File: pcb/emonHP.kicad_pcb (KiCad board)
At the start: 4 copper layers, 55 x 40 mm, 66 parts, among them J1 USB_C_Receptacle_USB2.0, J3 Screw_Terminal_01x03, J4 Screw_Terminal_01x02, J5 Screw_Terminal_01x02, J6 Screw_Terminal_01x03, J7 SJ-3524-SMT-TR, J8 Conn_ARM_JTAG_SWD_10, Q1 BC846, Q2 BSS84, Q3 BC846, SW1 SW_Push, U1 THVD1400D, U2 LM4040DBZ-5, U3 USBLC6-2P6, U4 AP2112K-3.3, U5 LM2733XMF, U6 ATSAMD21E15A-M, U7 MC33072

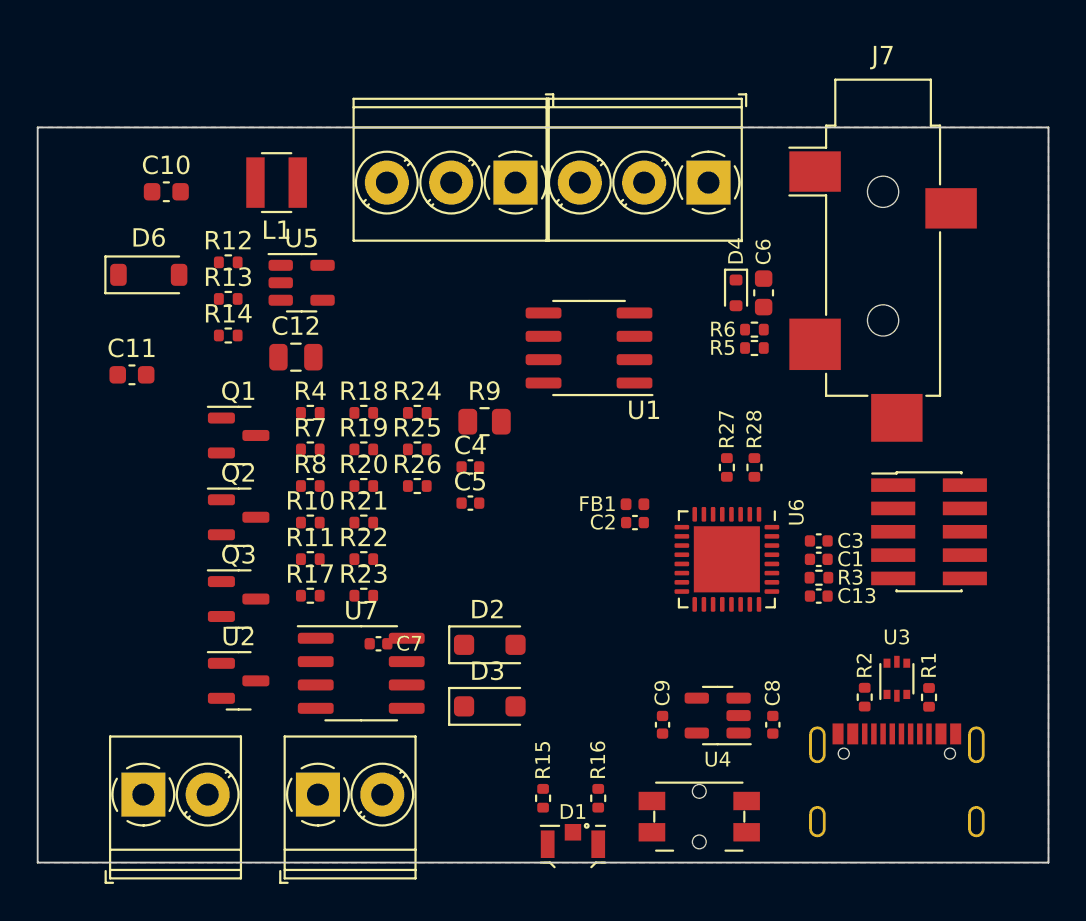
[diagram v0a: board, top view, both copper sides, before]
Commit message: * Work in progress
  - Add generate script
  - Add switch model
  - Start routing
  - Tidy schematic
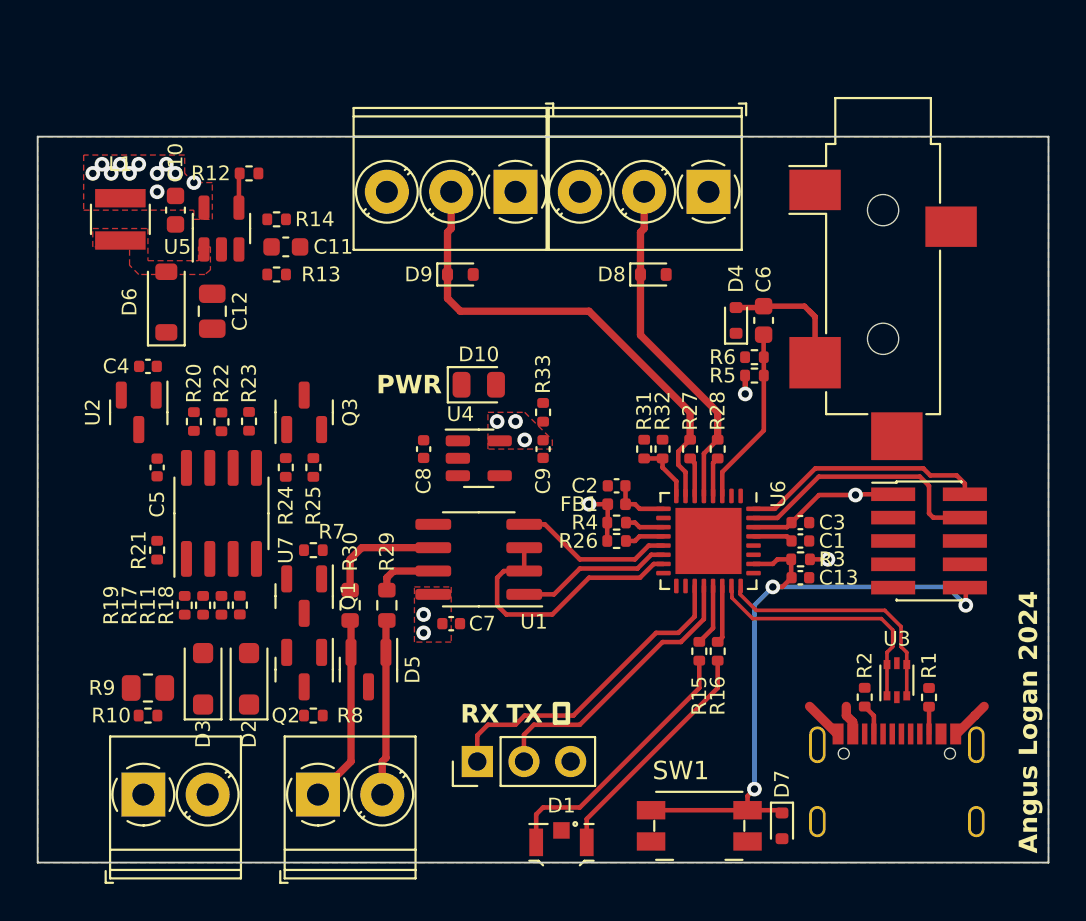
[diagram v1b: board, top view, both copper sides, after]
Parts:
- added D10: LED, LED_SMD:LED_0805_2012Metric, F.Cu at (124.0, 74.0)
- added D5: CDSOT23-SM712, Package_TO_SOT_SMD:SOT-23, F.Cu at (118.0, 89.5)
- added D7: ESD5Z3.3T5G, Diode_SMD:D_SOD-523, F.Cu at (140.5, 98.0)
- added D8: ESD5Z3.3T5G, Diode_SMD:D_SOD-523, F.Cu at (133.5, 68.0)
- added D9: ESD5Z3.3T5G, Diode_SMD:D_SOD-523, F.Cu at (123.0, 68.0)
- added J2: Conn_01x03, Connector_PinHeader_2.54mm:PinHeader_1x03_P2.54mm_Vertical, F.Cu at (123.9, 94.5)
- added R29: 10R, Resistor_SMD:R_0603_1608Metric, F.Cu at (119.0, 86.0)
- added R30: 10R, Resistor_SMD:R_0603_1608Metric, F.Cu at (117.0, 86.0)
- added R31: 20K, Resistor_SMD:R_0402_1005Metric, F.Cu at (133.0, 77.5)
- added R32: 1K, Resistor_SMD:R_0402_1005Metric, F.Cu at (134.0, 77.5)
- added R33: 1K, Resistor_SMD:R_0402_1005Metric, F.Cu at (127.5, 75.5)
- SW1: footprint Button_Switch_SMD:Panasonic_EVQPUM_EVQPUD -> Button_Switch_SMD:Panasonic_EVQPUJ_EVQPUA
- moved C8 24.2 mm to (121.0, 77.5), turned to -90 degrees
- moved R9 23.4 mm to (106.0, 90.5), turned to 180 degrees
- moved U4 19.1 mm to (124.0, 78.0), turned to 0 degrees
- moved C4 18.4 mm to (106.0, 73.0), turned to 180 degrees
- moved R4 17.7 mm to (131.5, 81.5), turned to 180 degrees
- moved C5 17.2 mm to (106.5, 78.5), turned to -90 degrees
- moved C9 16.3 mm to (127.5, 77.5), turned to -90 degrees
- moved D3 15.7 mm to (109.0, 90.0), turned to 90 degrees
- moved U2 15.6 mm to (105.5, 75.5), turned to -90 degrees
- moved R10 13.7 mm to (106.0, 92.0), turned to 180 degrees
- moved D2 13.2 mm to (111.5, 90.0), turned to 90 degrees
- moved U1 13.0 mm to (124.0, 83.5)
- moved R19 12.9 mm to (108.0, 86.0), turned to 90 degrees
- moved R8 12.5 mm to (115.0, 92.0)
- moved R18 12.4 mm to (111.0, 86.0), turned to -90 degrees
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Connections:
- net Net-(R19-Pad2) renamed /mbus/DIFF_5V
- R12 pad 1: +5V -> /BOOST_EN
- R12 pad 2: Net-(U5-EN) -> GND
- U1 pad 6: /RS485_B -> Net-(U1-A)
- U1 pad 7: /RS485_A -> Net-(U1-B)
- U5 pad 4: Net-(U5-EN) -> /BOOST_EN
- U6 pad 1: /CT1 -> unconnected-(U6-PA00-Pad1)
- U6 pad 16: unconnected-(U6-PA15-Pad16) -> /BOOST_EN
- U6 pad 19: unconnected-(U6-PA18-Pad19) -> /DBG_TX
- U6 pad 2: /OW_PU0 -> unconnected-(U6-PA01-Pad2)
- U6 pad 20: unconnected-(U6-PA19-Pad20) -> /DBG_RX
- U6 pad 3: /OPA0 -> /CT1
- U6 pad 4: /OW_PU1 -> /OW_PU0
- U6 pad 5: /OPA1 -> /OPA0
- U6 pad 6: unconnected-(U6-PA05-Pad6) -> /OW_PU1
- U6 pad 7: unconnected-(U6-PA06-Pad7) -> /OPA1
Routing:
- net +3V3: track 0.00 -> 52.2 mm, vias 0 -> 7
- net /~{RESET}: track 0.00 -> 36.2 mm, vias 0 -> 3
- net /OPA1: track 0.00 -> 26.6 mm
- net /OPA0: track 0.00 -> 18.7 mm
- net /DBG_TX: track 0.00 -> 17.6 mm
- net /DBG_RX: track 0.00 -> 15.7 mm
- net Net-(D1-K2): track 0.00 -> 14.8 mm
- net /RS485_DE: track 0.00 -> 14.8 mm
- net /SWCLK: track 0.00 -> 14.2 mm
- net /USB-DP: track 0.00 -> 13.8 mm
- net /USB-DN: track 0.00 -> 13.8 mm
- net /SWDIO: track 0.00 -> 13.3 mm
- net Net-(D1-K1): track 0.00 -> 12.9 mm
- net /RS485_B: track 0.00 -> 10.2 mm
- net /CT1: track 0.00 -> 9.72 mm
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- added copper zone on F.Cu, net +3V3
- added copper zone on In2.Cu, net +3V3
- added copper zone on F.Cu, net +5V
- added copper zone on In2.Cu, net +5V
- added copper zone on F.Cu, net /boost/BOOST_SW
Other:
- board size 55 x 40 mm -> 55 x 39.5 mm
- board text added: "Angus Logan 2024"
- board text added: "PWR"
- board text added: "RX"
- board text added: "TX"
- board text added: "emonHP OpenEnergyMonitor.org"
- board text added: "⏚"

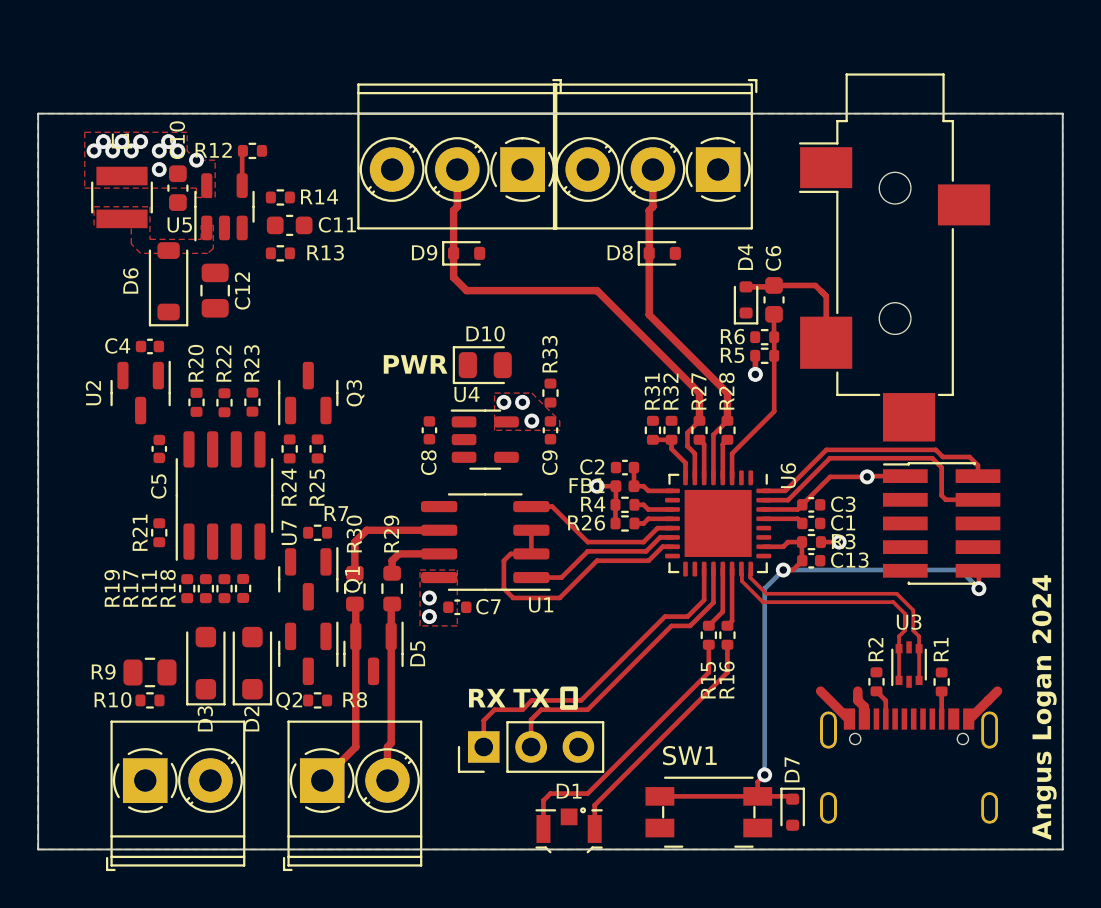
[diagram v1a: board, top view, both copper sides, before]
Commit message: * [0.1-dev] Voltage good
  - Add 36V voltage good detection
  - Add all 3D models
  - Correct footprint for front LED
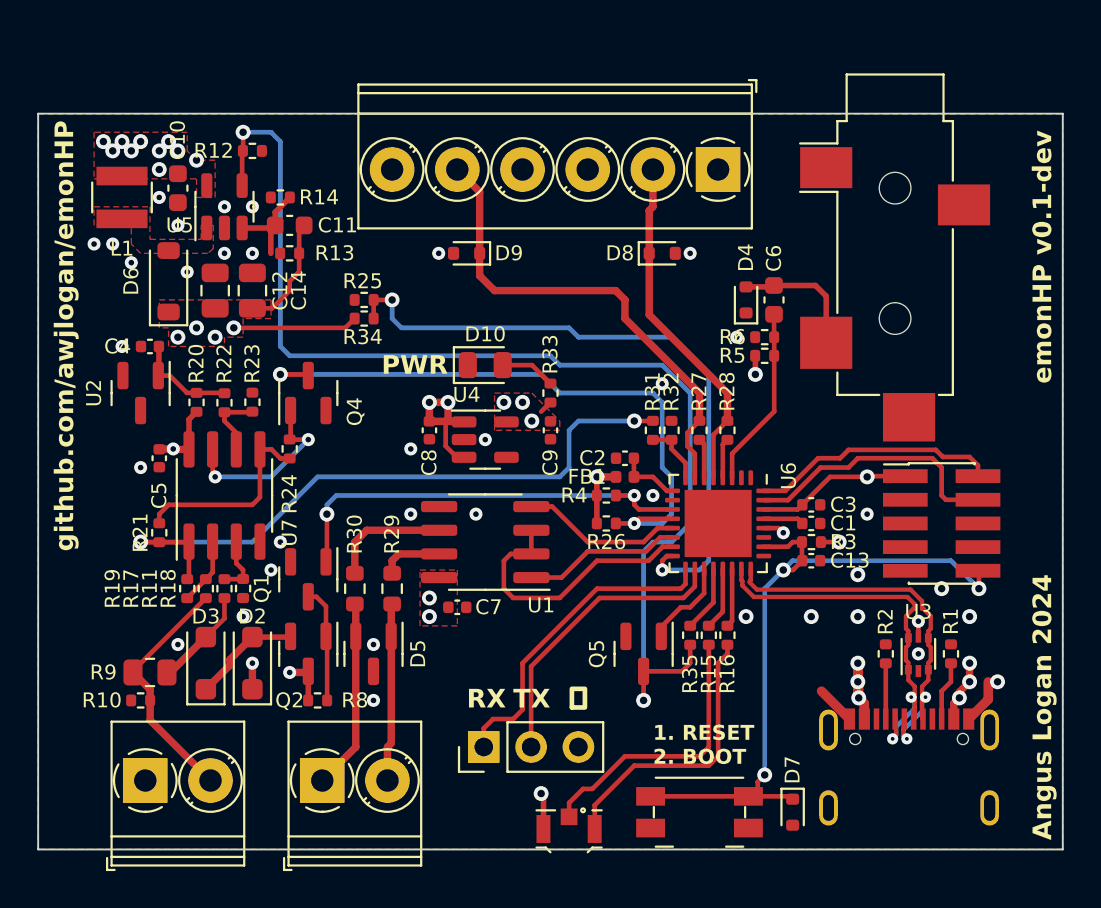
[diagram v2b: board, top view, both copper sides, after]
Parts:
- removed J3, J6: Screw_Terminal_01x03, TerminalBlock_Phoenix:TerminalBlock_Phoenix_PT-1,5-3-3.5-H_1x03_P3.50mm_Horizontal
- removed Q3: BC846, Package_TO_SOT_SMD:SOT-23
- removed R7: 10K, Resistor_SMD:R_0402_1005Metric
- added C14: 4u7, Capacitor_SMD:C_0805_2012Metric, F.Cu at (111.5, 70.0)
- added J9: Screw_Terminal_01x06, TerminalBlock_Phoenix:TerminalBlock_Phoenix_PT-1,5-6-3.5-H_1x06_P3.50mm_Horizontal, F.Cu at (136.5, 63.5)
- added Q4: Q_NPN_BEC_BRT, Package_TO_SOT_SMD:SOT-23, F.Cu at (114.5, 75.5)
- added Q5: Q_NPN_BEC_BRT, Package_TO_SOT_SMD:SOT-23, F.Cu at (132.5, 89.5)
- added R34: 180K, Resistor_SMD:R_0402_1005Metric, F.Cu at (117.5, 71.5)
- added R35: 3K3, Resistor_SMD:R_0402_1005Metric, F.Cu at (135.0, 88.5)
- D1: value LED_Dual_KAK -> LTST-S326KGJRKT; footprint LED_SMD:LED_LiteOn_LTST-S326 -> ltst-s326:LTST-S326
- Q1: value BC846 -> Q_NPN_BEC_BRT
- R25: value 20K -> 13K3
- R5: value 47K -> 100K
- moved R25 8.38 mm to (117.5, 70.5), turned to 180 degrees
- moved R1 1.59 mm to (149.0, 89.5)
- moved R2 1.58 mm to (145.5, 89.5)
- moved R4 1.12 mm to (130.5, 81.0)
- moved R26 1.00 mm to (130.5, 82.5)
- moved U3 0.76 mm to (147.2, 89.5)
- moved C2 0.50 mm to (131.5, 79.0)
- moved C5 0.50 mm to (106.5, 79.0)
- moved FB1 0.50 mm to (131.5, 80.0)
- moved R10 0.50 mm to (105.5, 92.0)
- moved R13 0.50 mm to (113.5, 68.0)
- moved SW1 0.50 mm to (135.5, 98.0)
- turned D9 to 180 degrees
- turned L1 to 90 degrees
- turned R24 to 90 degrees
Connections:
- D1 pad 2: +3V3 -> +5V
- L1 pad 1: +5V -> /boost/BOOST_SW
- L1 pad 2: /boost/BOOST_SW -> +5V
- Q1 pad 1: Net-(Q1-B) -> /MBUS_TX
- R12 pad 1: /BOOST_EN -> /BOOST_EN_PROT
- R24 pad 2: Net-(R24-Pad2) -> Net-(Q4-B)
- R25 pad 1: Net-(Q3-B) -> /36V_RG
- R25 pad 2: Net-(R24-Pad2) -> GND
- U5 pad 4: /BOOST_EN -> /BOOST_EN_PROT
- U6 pad 16: /BOOST_EN -> /36V_RG
- U6 pad 17: unconnected-(U6-PA16-Pad17) -> /DBG_TX
- U6 pad 18: unconnected-(U6-PA17-Pad18) -> /DBG_RX
- U6 pad 19: /DBG_TX -> /OC_CMP_OUT
- U6 pad 20: /DBG_RX -> /BOOST_EN
- U7 pad 7: Net-(R24-Pad2) -> Net-(Q4-B)
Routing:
- net /BOOST_EN_PROT: track 0.00 -> 62.4 mm, vias 0 -> 2
- net /mbus/DIFF_5V: track 0.00 -> 35.8 mm, vias 0 -> 2
- net /36V_RG: track 0.00 -> 35.1 mm, vias 0 -> 2
- net /MBUS_RX: track 2.14 -> 34.1 mm, vias 0 -> 2
- net +5V: track 1.64 -> 31.1 mm, vias 13 -> 22
- net /MBUS_TX: track 2.14 -> 23.4 mm, vias 0 -> 2
- net /36V: track 0.00 -> 20.6 mm, vias 0 -> 7
- net /MBUS_A: track 0.00 -> 13.1 mm
- net Net-(U7B-+): track 0.00 -> 10.6 mm
- net Net-(Q4-B): track 0.00 -> 9.85 mm, vias 0 -> 2
- net /USB-DN: track 13.8 -> 21.4 mm, vias 0 -> 2
- net /USB-DP: track 13.8 -> 21.4 mm, vias 0 -> 2
- net Net-(Q1-C): track 0.00 -> 6.15 mm
- net Net-(D2-A): track 0.00 -> 5.85 mm
- net Net-(U2-K): track 0.00 -> 5.45 mm
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- added copper zone on F.Cu, net /36V
- added copper zone on In2.Cu, net /36V
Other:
- board text added: "1. RESET 2. BOOT"
- board text added: "emonHP v0.1-dev"
- board text added: "github.com/awjlogan/emonHP"

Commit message: * [0.1-dev] Add git commit references and README
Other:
- board text added: "gitrev"
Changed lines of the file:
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@@
   (gr_line (start 155 100) (end 155 60.5)
     (stroke (width 0.1) (type default)) (layer "Edge.Cuts"))
-  (gr_text "github.com/awjlogan/emonHP" (at 102 84 90) (layer "F.SilkS")
+  (gr_text "github.com/awjlogan/emonHP" (at 101.5 99.5 90) (layer "F.SilkS")
     (effects (font (size 1 1) (thickness 0.25) bold) (justify left bottom))
   )
@@
     (effects (font (size 1 1) (thickness 0.25) bold) (justify left bottom))
   )
+  (gr_text "gitrev" (at 101.5 66 90) (layer "F.SilkS")
+    (effects (font (size 1 1) (thickness 0.25) bold) (justify left bottom))
+  )

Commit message: * Swap reset button for cheap onboard
  - Can access bootloader from serial, no need for front panel
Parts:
- SW1: footprint Button_Switch_SMD:Panasonic_EVQPUJ_EVQPUA -> Button_Switch_SMD:SW_Tactile_SPST_NO_Straight_CK_PTS636Sx25SMTRLFS
- moved D7 9.12 mm to (142.0, 89.0), turned to 0 degrees
- moved R15 7.57 mm to (135.0, 96.0)
- moved R16 7.57 mm to (136.0, 96.0)
- moved D1 6.50 mm to (135.0, 98.9)
- moved SW1 6.40 mm to (139.5, 93.0), turned to 90 degrees
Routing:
- net Net-(D1-K2): track 15.0 -> 1.74 mm
- net /~{RESET}: track 36.3 -> 23.5 mm
- net Net-(D1-K1): track 15.3 -> 2.55 mm
- net /LED_FP0: track 3.35 -> 11.3 mm
- net /LED_FP1: track 3.14 -> 11.1 mm
- net +5V: track 31.1 -> 27.5 mm
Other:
- board text added: "RESET"
- board text removed: "1. RESET 2. BOOT"

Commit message: [v0.1-dev] First pass on emonPi format
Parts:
- removed D1: LTST-S326KGJRKT, ltst-s326:LTST-S326
- removed D10: LED, LED_SMD:LED_0805_2012Metric
- removed D6: MBR0550, Diode_SMD:D_SOD-123
- removed J7: SJ-3524-SMT-TR, Connector_Audio:Jack_3.5mm_CUI_SJ-3524-SMT_Horizontal
- removed J8: Conn_ARM_JTAG_SWD_10, Connector_PinHeader_1.27mm:PinHeader_2x05_P1.27mm_Vertical_SMD
- removed J9: Screw_Terminal_01x06, TerminalBlock_Phoenix:TerminalBlock_Phoenix_PT-1,5-6-3.5-H_1x06_P3.50mm_Horizontal
- removed Q4, Q5: Q_NPN_BEC_BRT, Package_TO_SOT_SMD:SOT-23
- removed R12: 47K, Resistor_SMD:R_0402_1005Metric
- removed R13: 383K, Resistor_SMD:R_0402_1005Metric
- removed R14, R25: 13K3, Resistor_SMD:R_0402_1005Metric
- removed R15, R16, R21, R22: 1K, Resistor_SMD:R_0402_1005Metric
- removed R23, R24: 180K, Resistor_SMD:R_0402_1005Metric
- added C15: 100n, Capacitor_SMD:C_0402_1005Metric, F.Cu at (178.5, 140.0)
- added C18: 2u2, Capacitor_SMD:C_0603_1608Metric, F.Cu at (140.5, 100.0)
- added C19: 82p, Capacitor_SMD:C_0603_1608Metric, F.Cu at (146.5, 105.0)
- added C20: 4u7, Capacitor_SMD:C_0805_2012Metric, F.Cu at (116.5, 109.0)
- added C21: 4u7, Capacitor_SMD:C_0805_2012Metric, F.Cu at (143.0, 105.5)
- added C22: 1n, Capacitor_SMD:C_0402_1005Metric, F.Cu at (132.5, 96.0)
- added C23: 100n, Capacitor_SMD:C_0402_1005Metric, F.Cu at (126.5, 97.0)
- added C24: 100n, Capacitor_SMD:C_0402_1005Metric, F.Cu at (119.5, 91.0)
- added CN1: CONN_03SCREW, TerminalBlock_Phoenix:TerminalBlock_Phoenix_PT-1,5-3-3.5-H_1x03_P3.50mm_Horizontal, F.Cu at (108.0, 108.5)
- added CN3: Screw_Terminal_01x02, TerminalBlock_Phoenix:TerminalBlock_Phoenix_PT-1,5-2-3.5-H_1x02_P3.50mm_Horizontal, F.Cu at (108.0, 98.0)
- added CN4: CONN_03SCREW, TerminalBlock_Phoenix:TerminalBlock_Phoenix_PT-1,5-3-3.5-H_1x03_P3.50mm_Horizontal, F.Cu at (108.0, 84.0)
- added CN5: Screw_Terminal_01x02, TerminalBlock_Phoenix:TerminalBlock_Phoenix_PT-1,5-2-5.0-H_1x02_P5.00mm_Horizontal, F.Cu at (108.0, 135.5)
- added FB2: FerriteBead, Resistor_SMD:R_0402_1005Metric, F.Cu at (180.0, 140.0)
- added FD1: FIDUCIAL1X2, Fiducial:Fiducial_0.75mm_Mask1.5mm, F.Cu at (117.5, 121.0)
- added FD2: FIDUCIAL1X2, Fiducial:Fiducial_0.75mm_Mask1.5mm, F.Cu at (189.0, 146.5)
- added FD3: FIDUCIAL1X2, Fiducial:Fiducial_0.75mm_Mask1.5mm, F.Cu at (182.0, 65.5)
- added H1: MountingHole, MountingHole:MountingHole_2.7mm_M2.5, F.Cu at (128.5, 75.0)
- added H2: MountingHole, MountingHole:MountingHole_2.7mm_M2.5, F.Cu at (128.5, 124.0)
- added H3: MountingHole, MountingHole:MountingHole_2.1mm, F.Cu at (163.5, 97.0)
- added J3: USB_C_Receptacle_USB2.0, valcon-usb:CSP-USC16-TR, F.Cu at (108.5, 72.5)
- added JP1: Jumper_2_Open, Jumper:SolderJumper-2_P1.3mm_Open_TrianglePad1.0x1.5mm, F.Cu at (144.2, 96.2)
- added LED1: LED_Dual_KAK, ltst-s326:LTST-S326, F.Cu at (188.8, 134.0)
- added Q3: Q_NPN_BEC_BRT, Package_TO_SOT_SMD:SOT-23, F.Cu at (130.0, 105.0)
- added R36: 100K, Resistor_SMD:R_0402_1005Metric, F.Cu at (119.0, 97.0)
- added R37: 20K, Resistor_SMD:R_0402_1005Metric, F.Cu at (129.0, 99.0)
- added R38: 1K, Resistor_SMD:R_0402_1005Metric, F.Cu at (122.0, 97.0)
- added R39: 1K, Resistor_SMD:R_0402_1005Metric, F.Cu at (129.0, 100.5)
- added R40: 180K, Resistor_SMD:R_0402_1005Metric, F.Cu at (129.0, 102.0)
- added R41: 180K, Resistor_SMD:R_0402_1005Metric, F.Cu at (126.5, 104.0)
- added R42: 47K, Resistor_SMD:R_0402_1005Metric, F.Cu at (141.0, 117.5)
- added R43: 20K, Resistor_SMD:R_0402_1005Metric, F.Cu at (119.0, 95.5)
- added R44: 1K, Resistor_SMD:R_0402_1005Metric, F.Cu at (119.0, 94.0)
- added R45: 10R, Resistor_SMD:R_0603_1608Metric, F.Cu at (114.0, 90.5)
- added R46: 10R, Resistor_SMD:R_0603_1608Metric, F.Cu at (114.0, 84.5)
- added R7: 10K, Resistor_SMD:R_0402_1005Metric, F.Cu at (167.5, 118.5)
- added SMA1: SMACONNECTOR, Connector_Coaxial:SMA_Amphenol_132203-12_Horizontal, F.Cu at (185.5, 141.0)
- added SW2: SW_Push, Button_Switch_SMD:SW_Tactile_SPST_NO_Straight_CK_PTS636Sx25SMTRLFS, F.Cu at (145.5, 89.5)
- added TP1: TestPoint, TestPoint:TestPoint_Pad_D1.0mm, F.Cu at (182.0, 130.5)
- added TP4: TestPoint, TestPoint:TestPoint_Pad_D1.0mm, F.Cu at (183.0, 116.5)
- added TP5: TestPoint, TestPoint:TestPoint_Pad_D1.0mm, F.Cu at (133.5, 129.0)
- added TP6: TestPoint, TestPoint:TestPoint_Pad_D1.0mm, F.Cu at (184.0, 130.5)
- added TP7: TestPoint, TestPoint:TestPoint_Pad_D1.0mm, F.Cu at (123.5, 130.5)
- added TP8: TestPoint, TestPoint:TestPoint_Pad_D1.0mm, F.Cu at (180.5, 107.5)
- added U10: SN74LVC1T45DRL, Package_TO_SOT_SMD:SOT-563, F.Cu at (125.0, 91.5)
- added U8: THVD1400D, Package_SO:SOIC-8_3.9x4.9mm_P1.27mm, F.Cu at (121.5, 87.5)
- added U9: USBLC6-2P6, Package_TO_SOT_SMD:SOT-666, F.Cu at (116.2, 72.8)
- C1, C8, C9: value 1u -> 100n
- C10: value 2u2 -> 100n; footprint Capacitor_SMD:C_0603_1608Metric -> Capacitor_SMD:C_0402_1005Metric
- C11: value 82p -> 100n; footprint Capacitor_SMD:C_0603_1608Metric -> Capacitor_SMD:C_0402_1005Metric
- C12: value 4u7 -> 1u; footprint Capacitor_SMD:C_0805_2012Metric -> Capacitor_SMD:C_0402_1005Metric
- C13, C2, C5, C7: value 100n -> 2u2; footprint Capacitor_SMD:C_0402_1005Metric -> Capacitor_SMD:C_0603_1608Metric
- C14: value 4u7 -> 2u2; footprint Capacitor_SMD:C_0805_2012Metric -> Capacitor_SMD:C_0603_1608Metric
- C3: value 100n -> 10u; footprint Capacitor_SMD:C_0402_1005Metric -> Capacitor_SMD:C_0603_1608Metric
- C4: value 1n -> 2u2; footprint Capacitor_SMD:C_0402_1005Metric -> Capacitor_SMD:C_0603_1608Metric
- C6: value 10uF -> 100n; footprint Capacitor_SMD:C_0603_1608Metric -> Capacitor_SMD:C_0402_1005Metric
- D2: value BZT52C12 -> ESD5Z3.3T5G; footprint Diode_SMD:D_SOD-123F -> Diode_SMD:D_SOD-523
- D3: value BZT52C2V7 -> ESD5Z3.3T5G; footprint Diode_SMD:D_SOD-123F -> Diode_SMD:D_SOD-523
- D4: value 5V -> ESD5Z3.3T5G
- D5: value CDSOT23-SM712 -> SM712_SOT23
- D7: value ESD5Z3.3T5G -> MBR0550; footprint Diode_SMD:D_SOD-523 -> Diode_SMD:D_SOD-123
- D8: value ESD5Z3.3T5G -> BZT52C12; footprint Diode_SMD:D_SOD-523 -> Diode_SMD:D_SOD-123F
- D9: value ESD5Z3.3T5G -> BZT52C2V7; footprint Diode_SMD:D_SOD-523 -> Diode_SMD:D_SOD-123F
- FB1: value FerriteBead_Small -> FerriteBead; footprint Inductor_SMD:L_0402_1005Metric -> Resistor_SMD:R_0402_1005Metric
- J1: value USB_C_Receptacle_USB2.0 -> CONN_04PTH; footprint valcon-usb:CSP-USC16-TR -> Connector_PinSocket_2.54mm:PinSocket_1x04_P2.54mm_Vertical
- J2: value Conn_01x03 -> CONN_04PTH; footprint Connector_PinHeader_2.54mm:PinHeader_1x03_P2.54mm_Vertical -> Connector_PinSocket_2.54mm:PinSocket_1x04_P2.54mm_Vertical
- J4: value Screw_Terminal_01x02 -> Conn_ARM_JTAG_SWD_10; footprint TerminalBlock_Phoenix:TerminalBlock_Phoenix_PT-1,5-2-3.5-H_1x02_P3.50mm_Horizontal -> Connector_PinHeader_1.27mm:PinHeader_2x05_P1.27mm_Vertical_SMD
- J5: value Screw_Terminal_01x02 -> Conn_02x20_Odd_Even; footprint TerminalBlock_Phoenix:TerminalBlock_Phoenix_PT-1,5-2-3.5-H_1x02_P3.50mm_Horizontal -> RPi-SMD:REF-182665
- Q2: value BSS84 -> FDN5618P
- R1: value 5K1 -> 4K7
- R10: value 100K -> 1K
- R11: value 20K -> 10K
- R17: value 20K -> 47K
- R18, R19: value 100K -> 4K7
- R2: value 5K1 -> 37.4K; footprint Resistor_SMD:R_0402_1005Metric -> Resistor_SMD:R_2512_6332Metric
- R20: value 20K -> 37.4K; footprint Resistor_SMD:R_0402_1005Metric -> Resistor_SMD:R_2512_6332Metric
- R27: value 3K3 -> 383K
- R28: value 3K3 -> 13K3
- R29, R30: value 10R -> 47K; footprint Resistor_SMD:R_0603_1608Metric -> Resistor_SMD:R_0402_1005Metric
- R3: value 10K -> 1K
- R31: value 20K -> 100R; footprint Resistor_SMD:R_0402_1005Metric -> Resistor_SMD:R_0805_2012Metric
- R32: value 1K -> 100K
- R33: value 1K -> 20K
- R34: value 180K -> 20K
- R35: value 3K3 -> 100K
- R4: value 47K -> 5K1
- R5: value 100K -> 5K1
- R6, R8: value 47K -> 1K
- R9: value 100R -> 1K; footprint Resistor_SMD:R_0805_2012Metric -> Resistor_SMD:R_0402_1005Metric
- SW1: footprint Button_Switch_SMD:SW_Tactile_SPST_NO_Straight_CK_PTS636Sx25SMTRLFS -> Button_Switch_THT:SW_PUSH_6mm
- U1: value THVD1400D -> HCPL-3700M; footprint Package_SO:SOIC-8_3.9x4.9mm_P1.27mm -> Package_DIP:SMDIP-8_W7.62mm
- U2: value LM4040DBZ-5 -> ATSAMD21G15B-A; footprint Package_TO_SOT_SMD:SOT-23 -> Package_QFP:TQFP-48_7x7mm_P0.5mm
- U3: value USBLC6-2P6 -> AP2112K-3.3; footprint Package_TO_SOT_SMD:SOT-666 -> Package_TO_SOT_SMD:SOT-23-5
- U4: value AP2112K-3.3 -> RFM69CW; footprint Package_TO_SOT_SMD:SOT-23-5 -> rfm69cw:RFM69CW
- U6: value ATSAMD21E15A-M -> LM4040DBZ-5; footprint Package_DFN_QFN:QFN-32-1EP_5x5mm_P0.5mm_EP3.6x3.6mm -> Package_TO_SOT_SMD:SOT-23
- moved C14 95.1 mm to (180.0, 136.0)
- moved R9 90.1 mm to (185.5, 133.0), turned to 0 degrees
- moved R17 85.6 mm to (178.5, 136.0)
- moved R8 82.3 mm to (185.5, 134.5)
- moved U4 75.5 mm to (168.5, 139.0), turned to 180 degrees
- moved D3 67.8 mm to (170.5, 118.5), turned to -90 degrees
- moved R19 64.3 mm to (167.0, 111.5), turned to 180 degrees
- moved R18 62.6 mm to (167.0, 114.0), turned to 180 degrees
- moved C3 59.9 mm to (121.5, 138.0), turned to -90 degrees
- moved R2 59.6 mm to (116.3, 141.5), turned to 0 degrees
- moved R20 59.5 mm to (116.3, 135.0), turned to 0 degrees
- moved C13 57.9 mm to (178.5, 129.0), turned to 180 degrees
- moved R6 54.9 mm to (169.0, 118.5), turned to -90 degrees
- moved U1 54.6 mm to (128.0, 138.0), turned to 0 degrees
- moved U2 52.5 mm to (157.5, 83.0), turned to 90 degrees
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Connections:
- C1 pad 1: Net-(U6-VDDCORE) -> +3V3
- C10 pad 1: +5V -> /Vuc
- C11 pad 1: /36V -> /Vuc
- C11 pad 2: Net-(U5-FB) -> GND
- C12 pad 1: /36V -> Net-(U2-VDDCORE)
- C13 pad 1: /~{RESET} -> +5V
- C14 pad 1: /36V -> +3V3
- C2 pad 1: Net-(U6-VDDANA) -> GND
- C2 pad 2: GND -> +5V
- C3 pad 1: +3V3 -> Net-(U1-DC+)
- C3 pad 2: GND -> Net-(U1-DC-)
- C4 pad 1: Net-(U2-K) -> GND
- C4 pad 2: GND -> +5V
- C5 pad 1: /36V -> GND
- C5 pad 2: GND -> +3V3
- C6 pad 1: Net-(D4-A2) -> /~{RESET}
- C6 pad 2: /CT1 -> GND
- C7 pad 1: +5V -> +3V3
- C8 pad 1: +5V -> /Vuc
- C9 pad 1: +3V3 -> /Vuc
- D2 pad 1: /36V -> /OPA1
- D2 pad 2: Net-(D2-A) -> GND
- D3 pad 1: Net-(D2-A) -> Net-(D3-K)
- D3 pad 2: Net-(D3-A) -> GND
- D4 pad 1: GND -> Net-(D4-K)
- D4 pad 2: Net-(D4-A2) -> GND
- D5 pad 1: /RS485_A -> /RS485/RS485_A
- D5 pad 2: /RS485_B -> /RS485/RS485_B
- D7 pad 1: /~{RESET} -> /MBus/36V
- D7 pad 2: GND -> /Boost/BOOST_SW
- D8 pad 1: /OPA0 -> /MBus/36V
- D8 pad 2: GND -> Net-(D8-A)
- D9 pad 1: /OPA1 -> Net-(D8-A)
- D9 pad 2: GND -> Net-(D9-A)
- FB1 pad 1: Net-(U6-VDDANA) -> +3V3
- FB1 pad 2: +3V3 -> /Vuc
- J2 pad 1: /DBG_TX -> /I2C_SDA
- J2 pad 2: /DBG_RX -> /I2C_SCL
- J2 pad 3: GND -> +3V3
- J4 pad 1: GND -> /Vuc
- J4 pad 2: /MBUS_A -> /SWDIO
- J5 pad 1: /RS485_B -> unconnected-(J5-Pin_1-Pad1)
- J5 pad 2: /RS485_A -> +5V
- L1 pad 1: /boost/BOOST_SW -> /Boost/BOOST_SW
- Q1 pad 1: /MBUS_TX -> /UART5_TX
- Q2 pad 2: Net-(D2-A) -> Net-(D8-A)
- Q2 pad 3: /36V -> /MBus/36V
- R1 pad 1: Net-(J1-CC2) -> /OPA1
- R1 pad 2: GND -> +3V3
- R10 pad 1: /MBUS_A -> Net-(D4-K)
- R10 pad 2: GND -> /~{RESET}
- R11 pad 1: Net-(U7A-+) -> /Vuc
- R11 pad 2: Net-(D3-A) -> /~{RESET}
- R17 pad 1: Net-(U7A--) -> /RFM_SEL
- R17 pad 2: /MBUS_A -> +3V3
- R18 pad 1: Net-(U7A-+) -> +3V3
- R18 pad 2: GND -> /I2C_SDA
- R19 pad 1: Net-(U7A--) -> +3V3
- R19 pad 2: /mbus/DIFF_5V -> /I2C_SCL
- R2 pad 1: Net-(J1-CC1) -> /ACDetect/AC1
- R2 pad 2: GND -> Net-(U1-AC1)
- R20 pad 1: Net-(U2-K) -> /ACDetect/AC0
- R20 pad 2: /36V -> Net-(U1-AC0)
- R26 pad 1: +3V3 -> /MBUS_EN
- R26 pad 2: /MBUS_RX -> GND
- R27 pad 1: /OW_PU1 -> /MBus/36V
- R27 pad 2: /OPA1 -> Net-(U5-FB)
- R28 pad 1: /OW_PU0 -> Net-(U5-FB)
- R28 pad 2: /OPA0 -> GND
- R29 pad 1: /RS485_A -> /UART5_TX
- R29 pad 2: Net-(U1-B) -> +3V3
- R3 pad 1: +3V3 -> Net-(U2-PA07)
- R3 pad 2: /~{RESET} -> /PI_3V3
- R30 pad 1: /RS485_B -> /MBus/36V
- R30 pad 2: Net-(U1-A) -> Net-(Q1-C)
- R31 pad 1: /mbus/DIFF_5V -> Net-(D9-A)
- R31 pad 2: /MBUS_OC -> /MBus/MBUS_A
- R32 pad 1: /MBUS_OC -> /MBus/MBUS_A
- R33 pad 1: +3V3 -> Net-(U7A-+)
- R33 pad 2: Net-(D10-A) -> Net-(D9-A)
- R34 pad 1: /36V -> Net-(U7A--)
- R34 pad 2: /36V_RG -> /MBus/MBUS_A
- R35 pad 1: /BOOST_EN -> Net-(U7A-+)
- R35 pad 2: /BOOST_EN_PROT -> GND
- R4 pad 1: /MBUS_TX -> GND
- R4 pad 2: +3V3 -> Net-(J3-CC2)
- R5 pad 1: +3V3 -> GND
- R5 pad 2: /CT1 -> Net-(J3-CC1)
- R6 pad 1: GND -> Net-(D3-K)
- R6 pad 2: /CT1 -> /~{LCD_BUTTON}
- R8 pad 1: /36V -> /~{LED_STATUS}
- R8 pad 2: Net-(Q1-C) -> Net-(LED1-K2)
- R9 pad 1: Net-(D3-A) -> /~{LED_PROG}
- R9 pad 2: /MBUS_A -> Net-(LED1-K1)
- SW1 pad 2: /~{RESET} -> Net-(D3-K)
- U1 pad 1: /RS485_RX -> Net-(U1-AC0)
- U1 pad 2: /RS485_DE -> Net-(U1-DC+)
- U1 pad 3: /RS485_DE -> Net-(U1-DC-)
- U1 pad 4: /RS485_TX -> Net-(U1-AC1)
- U1 pad 6: Net-(U1-A) -> /DHW_SENSE
- U1 pad 7: Net-(U1-B) -> (no net)
- U1 pad 8: +5V -> +3V3
- U2 pad 1: Net-(U2-K) -> /OPA1
- U2 pad 2: GND -> /DHW_SENSE
- U2 pad 3: (no net) -> unconnected-(U2-PA02-Pad3)
- U3 pad 1: /USB-DN -> +5V
- U3 pad 3: /USB-DP -> +5V
- U3 pad 4: /USB-DP -> unconnected-(U3-NC-Pad4)
- U3 pad 5: +5V -> +3V3
- U4 pad 1: +5V -> Net-(SMA1-In)
- U4 pad 2: GND -> Net-(U4-VDD)
- U4 pad 3: +5V -> GND
- U4 pad 5: +3V3 -> /RFM_MOSI
- U5 pad 1: /boost/BOOST_SW -> /Boost/BOOST_SW
- U5 pad 4: /BOOST_EN_PROT -> /MBUS_EN
- U6 pad 1: unconnected-(U6-PA00-Pad1) -> Net-(U6-K)
- U6 pad 2: unconnected-(U6-PA01-Pad2) -> GND
- U6 pad 3: /CT1 -> (no net)
- U7 pad 1: /mbus/DIFF_5V -> /MBus/DIFF_5V
- U7 pad 8: /36V -> /MBus/36V
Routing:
- net +3V3: track 53.3 -> 273.4 mm
- net +5V: track 27.5 -> 238.1 mm, vias 22 -> 3
- net /UART5_TX: track 0.00 -> 122.3 mm, vias 0 -> 2
- net /UART3_TX: track 0.00 -> 122.0 mm, vias 0 -> 5
- net /UART5_RX: track 0.00 -> 114.3 mm, vias 0 -> 2
- net /UART3_RTS: track 0.00 -> 108.3 mm, vias 0 -> 3
- net /UART3_RX: track 0.00 -> 103.6 mm, vias 0 -> 3
- net /I2C_SDA: track 0.00 -> 83.2 mm, vias 0 -> 2
- net /RFM_MOSI: track 0.00 -> 81.7 mm, vias 0 -> 2
- net /I2C_SCL: track 0.00 -> 81.1 mm, vias 0 -> 1
- net /DHW_SENSE: track 0.00 -> 75.7 mm
- net /RFM_SCK: track 0.00 -> 73.1 mm
- net /RFM_SEL: track 0.00 -> 72.1 mm
- net /BOOST_EN_PROT: track 62.4 -> 0.00 mm, vias 2 -> 0
- net /RFM_MISO: track 0.00 -> 62.3 mm, vias 0 -> 2
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- added copper zone on F.Cu, net /Boost/BOOST_SW
- added copper zone on F.Cu, net /MBus/36V
- removed copper zone on F.Cu, net +3V3
- removed copper zone on In2.Cu, net +3V3
- removed copper zone on In2.Cu, net +5V
- removed copper zone on F.Cu, net /36V
- removed copper zone on In2.Cu, net /36V
- removed copper zone on F.Cu, net /boost/BOOST_SW
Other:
- board size 55 x 39.5 mm -> 85 x 88 mm
- board text added: "####"
- board text added: "1: RESET 2: BOOT"
- board text added: "3V3"
- board text added: "5V"
- board text added: "Angus Logan 2025"
- board text added: "Designed and assembled in the UK"
- board text added: "GND"
- board text added: "Lead free PCB RoHS components"
- board text added: "OLED"
- board text added: "OpenEnergyMonitor.org"
- board text added: "QC"
- board text added: "SCL"
- board text added: "SDA"
- board text added: "V_{USB}"
- board text added: "emonHP1"
- board text added: "v0.1 (gitrev)"
- board text added: "⚡"
- board text removed: "Angus Logan 2024"
- board text removed: "PWR"
- board text removed: "RESET"
- board text removed: "RX"
- board text removed: "TX"
- board text removed: "emonHP OpenEnergyMonitor.org"
- board text removed: "emonHP v0.1-dev"
- board text removed: "gitrev"
